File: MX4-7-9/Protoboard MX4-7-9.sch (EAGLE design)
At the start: 444 parts, among them J1 DCJ0202

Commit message: Update to rev2
Updated to Pin headers instead of single wire pads
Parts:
- removed PAD1, PAD10, PAD100, PAD101, PAD102, PAD103, PAD104, PAD105, PAD106, PAD107, PAD108, PAD109, PAD11, PAD110, PAD111, PAD112, PAD113, PAD114, PAD115, PAD116, PAD117, PAD118, PAD119, PAD12, PAD120, PAD121, PAD122, PAD123, PAD124, PAD125, PAD126, PAD127, PAD128, PAD129, PAD13, PAD130, PAD131, PAD132, PAD133, PAD134, PAD135, PAD136, PAD137, PAD138, PAD139, PAD14, PAD140, PAD141, PAD142, PAD143, PAD144, PAD145, PAD146, PAD147, PAD148, PAD149, PAD15, PAD150, PAD151, PAD152, PAD153, PAD154, PAD155, PAD156, PAD157, PAD158, PAD159, PAD16, PAD160, PAD161, PAD162, PAD163, PAD164, PAD165, PAD166, PAD167, PAD168, PAD169, PAD17, PAD170, PAD171, PAD172, PAD173, PAD174, PAD175, PAD176, PAD177, PAD178, PAD179, PAD18, PAD180, PAD181, PAD182, PAD183, PAD184, PAD185, PAD186, PAD187, PAD188, PAD189, PAD19, PAD190, PAD191, PAD192, PAD193, PAD194, PAD195, PAD196, PAD197, PAD198, PAD199, PAD2, PAD20, PAD200, PAD201, PAD202, PAD203, PAD204, PAD205, PAD206, PAD207, PAD208, PAD209, PAD21, PAD210, PAD211, PAD212, PAD213, PAD214, PAD215, PAD216, PAD217, PAD218, PAD219, PAD22, PAD220, PAD221, PAD222, PAD223, PAD224, PAD225, PAD226, PAD227, PAD228, PAD229, PAD23, PAD230, PAD231, PAD232, PAD233, PAD234, PAD235, PAD236, PAD237, PAD238, PAD239, PAD24, PAD240, PAD25, PAD26, PAD260, PAD261, PAD262, PAD263, PAD264, PAD265, PAD266, PAD269, PAD27, PAD270, PAD271, PAD272, PAD273, PAD274, PAD275, PAD276, PAD277, PAD278, PAD279, PAD28, PAD280, PAD281, PAD282, PAD283, PAD284, PAD285, PAD286, PAD287, PAD288, PAD289, PAD29, PAD290, PAD291, PAD292, PAD293, PAD294, PAD295, PAD296, PAD297, PAD298, PAD299, PAD3, PAD30, PAD300, PAD301, PAD302, PAD303, PAD304, PAD305, PAD306, PAD307, PAD308, PAD309, PAD31, PAD310, PAD311, PAD312, PAD313, PAD314, PAD315, PAD316, PAD317, PAD318, PAD319, PAD32, PAD320, PAD321, PAD322, PAD323, PAD324, PAD325, PAD326, PAD327, PAD328, PAD329, PAD33, PAD330, PAD331, PAD332, PAD333, PAD334, PAD335, PAD336, PAD337, PAD338, PAD339, PAD34, PAD340, PAD341, PAD342, PAD343, PAD344, PAD345, PAD346, PAD347, PAD348, PAD349, PAD35, PAD350, PAD351, PAD352, PAD353, PAD354, PAD355, PAD356, PAD357, PAD358, PAD359, PAD36, PAD360, PAD361, PAD362, PAD363, PAD364, PAD365, PAD366, PAD367, PAD368, PAD369, PAD37, PAD370, PAD371, PAD372, PAD373, PAD374, PAD375, PAD376, PAD377, PAD378, PAD379, PAD38, PAD380, PAD381, PAD382, PAD383, PAD384, PAD385, PAD386, PAD387, PAD388, PAD389, PAD39, PAD390, PAD391, PAD392, PAD393, PAD394, PAD395, PAD4, PAD40, PAD41, PAD414, PAD415, PAD416, PAD42, PAD420, PAD421, PAD422, PAD423, PAD424, PAD425, PAD426, PAD427, PAD428, PAD429, PAD43, PAD430, PAD431, PAD432, PAD433, PAD434, PAD435, PAD436, PAD437, PAD438, PAD439, PAD44, PAD440, PAD441, PAD442, PAD443, PAD444, PAD445, PAD446, PAD447, PAD448, PAD449, PAD45, PAD450, PAD451, PAD452, PAD453, PAD454, PAD455, PAD456, PAD457, PAD458, PAD459, PAD46, PAD460, PAD461, PAD462, PAD463, PAD464, PAD465, PAD466, PAD467, PAD468, PAD469, PAD47, PAD470, PAD48, PAD49, PAD5, PAD50, PAD51, PAD52, PAD53, PAD54, PAD55, PAD56, PAD57, PAD58, PAD59, PAD6, PAD60, PAD61, PAD62, PAD63, PAD64, PAD65, PAD66, PAD67, PAD68, PAD69, PAD7, PAD70, PAD71, PAD72, PAD73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: (no value), wirepad:1,6/0,8
- removed PAD471, PAD472, PAD473, PAD474, PAD475, PAD476, PAD477, PAD481, PAD482, PAD483, PAD484, PAD485, PAD486, PAD487: WIREPAD3,17/1,3, wirepad:WIREPAD3,17/1,3
- added J2, J3: (no value), SparkFun-Connectors:M29NO_SILK
- added J4, J5: (no value), SparkFun-Connectors:M20NO_SILK_KIT
- added J6, J7: (no value), SparkFun-Connectors:M05NO_SILK
- added JP1: USB-RECEPTABLE, daspilker:USB-RECEPTABLE
- added JP10, JP11, JP12, JP13, JP14, JP15, JP16, JP17, JP18, JP19, JP2, JP20, JP21, JP22, JP23, JP24, JP25, JP26, JP27, JP28, JP29, JP3, JP30, JP31, JP32, JP33, JP4, JP47, JP5, JP6, JP64, JP65, JP66, JP67, JP68, JP69, JP7, JP70, JP71, JP72, JP73, JP74, JP75, JP76, JP77, JP78, JP79, JP8, JP80, JP81, JP82, JP83, JP9: (no value), adafruit:PINHD-1X6CB
- added JP100, JP101, JP102, JP103, JP104, JP105, JP106, JP107, JP108, JP109, JP34, JP35, JP36, JP37, JP38, JP39, JP40, JP41, JP42, JP43, JP44, JP45, JP46, JP48, JP49, JP50, JP51, JP52, JP53, JP54, JP55, JP56, JP57, JP58, JP59, JP60, JP61, JP62, JP63, JP85, JP86, JP87, JP88, JP89, JP90, JP91, JP92, JP93, JP96, JP97, JP98, JP99: (no value), adafruit:PINHD-1X1CB
- added U2: (no value), SparkFun-PowerIC:MIC52053.3V
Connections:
- removed net N$25: PAD104.P, PAD105.P, PAD113.P, PAD114.P, PAD87.P, PAD95.P, PAD96.P
- removed net N$40: PAD377.P, PAD378.P, PAD379.P, PAD380.P, PAD381.P, PAD382.P, PAD383.P
- removed net N$45: PAD185.P, PAD186.P, PAD194.P, PAD195.P, PAD203.P, PAD204.P, PAD212.P
- removed net N$60: PAD375.P, PAD376.P, PAD384.P, PAD390.P, PAD395.P, PAD414.P, PAD415.P
- removed net N$61: PAD416.P, PAD420.P, PAD437.P, PAD438.P, PAD457.P, PAD458.P, PAD463.P
- removed net N$62: PAD464.P, PAD465.P, PAD466.P, PAD467.P, PAD468.P, PAD469.P, PAD470.P
- removed net N$63: PAD471.P, PAD487.P
- removed net N$64: PAD472.P, PAD486.P
- removed net N$65: PAD473.P, PAD485.P
- removed net N$66: PAD474.P, PAD484.P
- removed net N$67: PAD475.P, PAD483.P
- removed net N$68: PAD476.P, PAD482.P
- removed net N$69: PAD477.P, PAD481.P
- new net N$2: JP31.1, JP31.2, JP31.3, JP31.4, JP31.5, JP31.6, JP96.1
- new net N$46: JP106.1, JP70.1, JP70.2, JP70.3, JP70.4, JP70.5, JP70.6
- new net N$47: JP107.1, JP71.1, JP71.2, JP71.3, JP71.4, JP71.5, JP71.6
- new net N$48: JP108.1, JP72.1, JP72.2, JP72.3, JP72.4, JP72.5, JP72.6
- new net N$52: JP76.1, JP76.2, JP76.3, JP76.4, JP76.5, JP76.6, JP87.1
- new net N$53: JP77.1, JP77.2, JP77.3, JP77.4, JP77.5, JP77.6, JP88.1
- new net N$54: JP78.1, JP78.2, JP78.3, JP78.4, JP78.5, JP78.6, JP89.1
- new net N$55: JP79.1, JP79.2, JP79.3, JP79.4, JP79.5, JP79.6, JP90.1
- new net N$56: JP80.1, JP80.2, JP80.3, JP80.4, JP80.5, JP80.6, JP91.1
- new net N$57: JP81.1, JP81.2, JP81.3, JP81.4, JP81.5, JP81.6, JP92.1
- new net N$58: JP82.1, JP82.2, JP82.3, JP82.4, JP82.5, JP82.6, JP93.1
- net GND: now also J2.1, J2.10, J2.11, J2.12, J2.13, J2.14, J2.15, J2.16, J2.17, J2.18, J2.19, J2.2, J2.20, J2.21, J2.22, J2.23, J2.24, J2.25, J2.26, J2.27, J2.28, J2.29, J2.3, J2.4, J2.5, J2.6, J2.7, J2.8, J2.9, J4.1, J4.10, J4.11, J4.12, J4.13, J4.14, J4.15, J4.16, J4.17, J4.18, J4.19, J4.2, J4.20, J4.3, J4.4, J4.5, J4.6, J4.7, J4.8, J4.9, J6.1, J6.2, J6.3, J6.4, J6.5, JP1.GND, U2.GND; no longer PAD17.P, PAD22.P, PAD23.P, PAD24.P, PAD25.P, PAD26.P, PAD27.P, PAD276.P, PAD277.P, PAD28.P, PAD285.P, PAD286.P, PAD29.P, PAD30.P, PAD31.P, PAD32.P, PAD326.P, PAD327.P, PAD328.P, PAD329.P, PAD33.P, PAD330.P, PAD331.P, PAD339.P, PAD36.P, PAD38.P, PAD4.P, PAD421.P, PAD422.P, PAD423.P, PAD424.P, PAD425.P, PAD426.P, PAD427.P, PAD428.P, PAD429.P, PAD430.P, PAD431.P, PAD432.P, PAD433.P, PAD434.P, PAD435.P, PAD436.P, PAD439.P, PAD440.P, PAD441.P
- net N$1: now also JP2.1, JP2.2, JP2.3, JP2.4, JP2.5, JP2.6, JP48.1; no longer PAD391.P, PAD392.P, PAD393.P, PAD394.P, PAD42.P, PAD43.P, PAD44.P
- net N$10: now also JP54.1, JP9.1, JP9.2, JP9.3, JP9.4, JP9.5, JP9.6; no longer PAD106.P, PAD107.P, PAD108.P, PAD109.P, PAD110.P, PAD111.P, PAD112.P
- net N$11: now also JP10.1, JP10.2, JP10.3, JP10.4, JP10.5, JP10.6, JP55.1; no longer PAD115.P, PAD116.P, PAD117.P, PAD118.P, PAD119.P, PAD120.P, PAD121.P
- net N$12: now also JP11.1, JP11.2, JP11.3, JP11.4, JP11.5, JP11.6, JP56.1; no longer PAD124.P, PAD125.P, PAD126.P, PAD127.P, PAD128.P, PAD129.P, PAD130.P
- net N$13: now also JP12.1, JP12.2, JP12.3, JP12.4, JP12.5, JP12.6, JP57.1; no longer PAD133.P, PAD134.P, PAD135.P, PAD136.P, PAD137.P, PAD138.P, PAD139.P
- net N$14: now also JP13.1, JP13.2, JP13.3, JP13.4, JP13.5, JP13.6, JP58.1; no longer PAD142.P, PAD143.P, PAD144.P, PAD145.P, PAD146.P, PAD147.P, PAD148.P
- net N$15: now also JP14.1, JP14.2, JP14.3, JP14.4, JP14.5, JP14.6, JP59.1; no longer PAD151.P, PAD152.P, PAD153.P, PAD154.P, PAD155.P, PAD156.P, PAD157.P
- net N$16: now also JP15.1, JP15.2, JP15.3, JP15.4, JP15.5, JP15.6, JP60.1; no longer PAD160.P, PAD161.P, PAD162.P, PAD163.P, PAD164.P, PAD165.P, PAD166.P
- net N$17: now also JP16.1, JP16.2, JP16.3, JP16.4, JP16.5, JP16.6, JP61.1; no longer PAD169.P, PAD170.P, PAD171.P, PAD172.P, PAD173.P, PAD174.P, PAD175.P
- net N$18: now also JP4.1, JP4.2, JP4.3, JP4.4, JP4.5, JP4.6, JP62.1; no longer PAD178.P, PAD179.P, PAD180.P, PAD181.P, PAD182.P, PAD183.P, PAD184.P
- net N$19: now also JP17.1, JP17.2, JP17.3, JP17.4, JP17.5, JP17.6, JP63.1; no longer PAD187.P, PAD188.P, PAD189.P, PAD190.P, PAD191.P, PAD192.P, PAD193.P
- net N$20: now also JP18.1, JP18.2, JP18.3, JP18.4, JP18.5, JP18.6, JP34.1; no longer PAD196.P, PAD197.P, PAD198.P, PAD199.P, PAD200.P, PAD201.P, PAD202.P
- net N$21: now also JP19.1, JP19.2, JP19.3, JP19.4, JP19.5, JP19.6, JP35.1; no longer PAD205.P, PAD206.P, PAD207.P, PAD208.P, PAD209.P, PAD210.P, PAD211.P
- net N$22: now also JP20.1, JP20.2, JP20.3, JP20.4, JP20.5, JP20.6, JP36.1; no longer PAD214.P, PAD215.P, PAD216.P, PAD217.P, PAD218.P, PAD219.P, PAD220.P
- net N$23: now also JP47.1, JP47.2, JP47.3, JP47.4, JP47.5, JP47.6, JP99.1; no longer PAD66.P, PAD67.P, PAD68.P, PAD69.P, PAD70.P, PAD71.P, PAD72.P
- net N$24: now also JP100.1, JP64.1, JP64.2, JP64.3, JP64.4, JP64.5, JP64.6; no longer PAD73.P, PAD74.P, PAD75.P, PAD76.P, PAD77.P, PAD78.P, PAD86.P
- net N$26: now also JP101.1, JP65.1, JP65.2, JP65.3, JP65.4, JP65.5, JP65.6; no longer PAD122.P, PAD123.P, PAD131.P, PAD132.P, PAD140.P, PAD141.P, PAD149.P
- net N$27: now also JP21.1, JP21.2, JP21.3, JP21.4, JP21.5, JP21.6, JP37.1; no longer PAD260.P, PAD261.P, PAD262.P, PAD263.P, PAD264.P, PAD265.P, PAD266.P
- net N$28: now also JP22.1, JP22.2, JP22.3, JP22.4, JP22.5, JP22.6, JP38.1; no longer PAD269.P, PAD270.P, PAD271.P, PAD272.P, PAD273.P, PAD274.P, PAD275.P
- net N$29: now also JP23.1, JP23.2, JP23.3, JP23.4, JP23.5, JP23.6, JP39.1; no longer PAD278.P, PAD279.P, PAD280.P, PAD281.P, PAD282.P, PAD283.P, PAD284.P
- net N$3: now also JP32.1, JP32.2, JP32.3, JP32.4, JP32.5, JP32.6, JP97.1; no longer PAD1.P, PAD2.P, PAD3.P, PAD34.P, PAD35.P, PAD37.P, PAD40.P
- net N$30: now also JP24.1, JP24.2, JP24.3, JP24.4, JP24.5, JP24.6, JP40.1; no longer PAD287.P, PAD288.P, PAD289.P, PAD290.P, PAD291.P, PAD292.P, PAD293.P
- net N$31: now also JP25.1, JP25.2, JP25.3, JP25.4, JP25.5, JP25.6, JP41.1; no longer PAD296.P, PAD297.P, PAD298.P, PAD299.P, PAD300.P, PAD301.P, PAD302.P
- net N$32: now also JP26.1, JP26.2, JP26.3, JP26.4, JP26.5, JP26.6, JP42.1; no longer PAD305.P, PAD306.P, PAD307.P, PAD308.P, PAD309.P, PAD310.P, PAD311.P
- net N$33: now also JP27.1, JP27.2, JP27.3, JP27.4, JP27.5, JP27.6, JP43.1; no longer PAD314.P, PAD315.P, PAD316.P, PAD317.P, PAD318.P, PAD319.P, PAD320.P
- net N$34: now also JP102.1, JP66.1, JP66.2, JP66.3, JP66.4, JP66.5, JP66.6; no longer PAD150.P, PAD158.P, PAD159.P, PAD167.P, PAD168.P, PAD176.P, PAD177.P
- net N$35: now also JP28.1, JP28.2, JP28.3, JP28.4, JP28.5, JP28.6, JP44.1; no longer PAD332.P, PAD333.P, PAD334.P, PAD335.P, PAD336.P, PAD337.P, PAD338.P
- net N$36: now also JP29.1, JP29.2, JP29.3, JP29.4, JP29.5, JP29.6, JP45.1; no longer PAD341.P, PAD342.P, PAD343.P, PAD344.P, PAD345.P, PAD346.P, PAD347.P
- net N$37: now also JP30.1, JP30.2, JP30.3, JP30.4, JP30.5, JP30.6, JP46.1; no longer PAD350.P, PAD351.P, PAD352.P, PAD353.P, PAD354.P, PAD355.P, PAD356.P
- net N$38: now also JP103.1, JP67.1, JP67.2, JP67.3, JP67.4, JP67.5, JP67.6; no longer PAD359.P, PAD360.P, PAD361.P, PAD362.P, PAD363.P, PAD364.P, PAD365.P
- net N$39: now also JP104.1, JP68.1, JP68.2, JP68.3, JP68.4, JP68.5, JP68.6; no longer PAD368.P, PAD369.P, PAD370.P, PAD371.P, PAD372.P, PAD373.P, PAD374.P
- net N$4: now also JP33.1, JP33.2, JP33.3, JP33.4, JP33.5, JP33.6, JP98.1; no longer PAD45.P, PAD46.P, PAD47.P, PAD48.P, PAD49.P, PAD50.P, PAD51.P
- net N$41: now also JP105.1, JP69.1, JP69.2, JP69.3, JP69.4, JP69.5, JP69.6; no longer PAD385.P, PAD386.P, PAD387.P, PAD388.P, PAD389.P, PAD39.P, PAD41.P
- net N$49: now also JP109.1, JP73.1, JP73.2, JP73.3, JP73.4, JP73.5, JP73.6; no longer PAD213.P, PAD221.P, PAD222.P, PAD223.P, PAD224.P, PAD225.P, PAD226.P
- net N$5: now also JP3.1, JP3.2, JP3.3, JP3.4, JP3.5, JP3.6, JP49.1; no longer PAD52.P, PAD53.P, PAD54.P, PAD55.P, PAD56.P, PAD57.P, PAD58.P
- net N$50: now also JP74.1, JP74.2, JP74.3, JP74.4, JP74.5, JP74.6, JP85.1; no longer PAD227.P, PAD228.P, PAD229.P, PAD230.P, PAD231.P, PAD232.P, PAD233.P
- net N$51: now also JP75.1, JP75.2, JP75.3, JP75.4, JP75.5, JP75.6, JP86.1; no longer PAD234.P, PAD235.P, PAD236.P, PAD237.P, PAD238.P, PAD239.P, PAD240.P
- net N$59: now also JP83.1, JP83.2, JP83.3, JP83.4, JP83.5, JP83.6; no longer PAD340.P, PAD348.P, PAD349.P, PAD357.P, PAD358.P, PAD366.P, PAD367.P
- net N$6: now also JP5.1, JP5.2, JP5.3, JP5.4, JP5.5, JP5.6, JP50.1; no longer PAD59.P, PAD60.P, PAD61.P, PAD62.P, PAD63.P, PAD64.P, PAD65.P
- net N$7: now also JP51.1, JP6.1, JP6.2, JP6.3, JP6.4, JP6.5, JP6.6; no longer PAD79.P, PAD80.P, PAD81.P, PAD82.P, PAD83.P, PAD84.P, PAD85.P
- net N$8: now also JP52.1, JP7.1, JP7.2, JP7.3, JP7.4, JP7.5, JP7.6; no longer PAD88.P, PAD89.P, PAD90.P, PAD91.P, PAD92.P, PAD93.P, PAD94.P
- net N$9: now also JP53.1, JP8.1, JP8.2, JP8.3, JP8.4, JP8.5, JP8.6; no longer PAD100.P, PAD101.P, PAD102.P, PAD103.P, PAD97.P, PAD98.P, PAD99.P
- net VCC: now also JP1.VCC, U2.EN, U2.IN
- net VDD: now also J3.1, J3.10, J3.11, J3.12, J3.13, J3.14, J3.15, J3.16, J3.17, J3.18, J3.19, J3.2, J3.20, J3.21, J3.22, J3.23, J3.24, J3.25, J3.26, J3.27, J3.28, J3.29, J3.3, J3.4, J3.5, J3.6, J3.7, J3.8, J3.9, J5.1, J5.10, J5.11, J5.12, J5.13, J5.14, J5.15, J5.16, J5.17, J5.18, J5.19, J5.2, J5.20, J5.3, J5.4, J5.5, J5.6, J5.7, J5.8, J5.9, J7.1, J7.2, J7.3, J7.4, J7.5, U2.OUT; no longer PAD10.P, PAD11.P, PAD12.P, PAD13.P, PAD14.P, PAD15.P, PAD16.P, PAD18.P, PAD19.P, PAD20.P, PAD21.P, PAD294.P, PAD295.P, PAD303.P, PAD304.P, PAD312.P, PAD313.P, PAD321.P, PAD322.P, PAD323.P, PAD324.P, PAD325.P, PAD442.P, PAD443.P, PAD444.P, PAD445.P, PAD446.P, PAD447.P, PAD448.P, PAD449.P, PAD450.P, PAD451.P, PAD452.P, PAD453.P, PAD454.P, PAD455.P, PAD456.P, PAD459.P, PAD460.P, PAD461.P, PAD462.P, PAD5.P, PAD6.P, PAD7.P, PAD8.P, PAD9.P
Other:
- moved on the sheet: J1

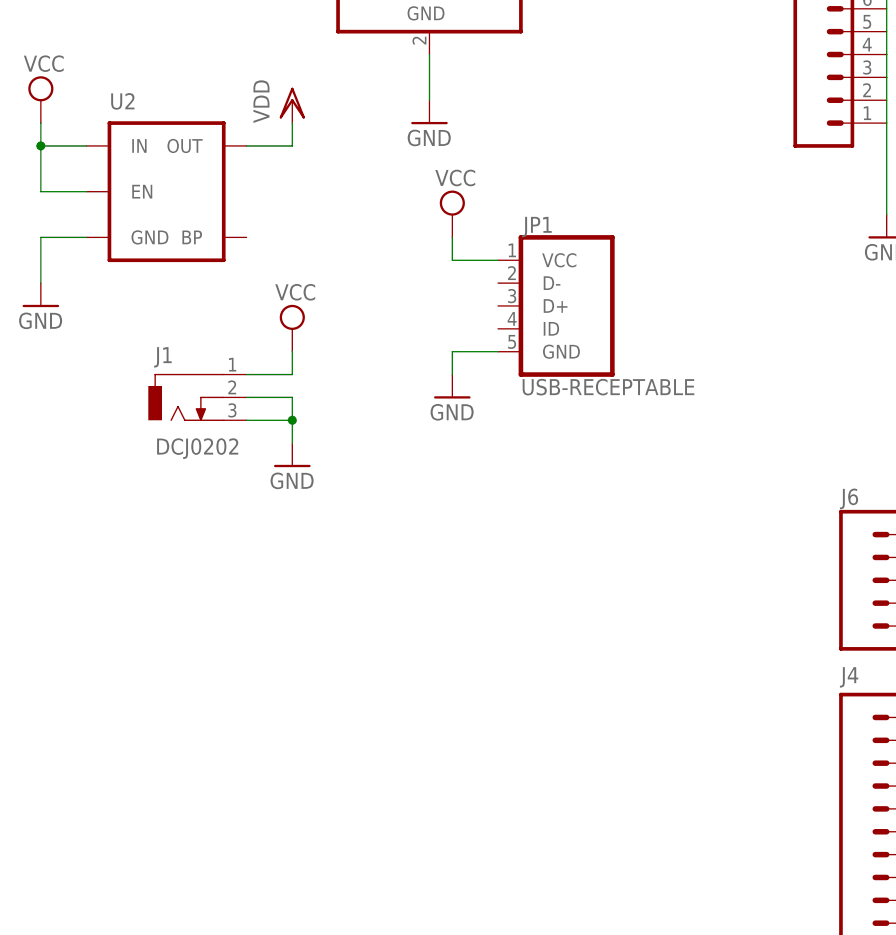
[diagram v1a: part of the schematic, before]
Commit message: Change usb connector
Change to correct usb connecter and moved esp8266 bit more onto the
board.
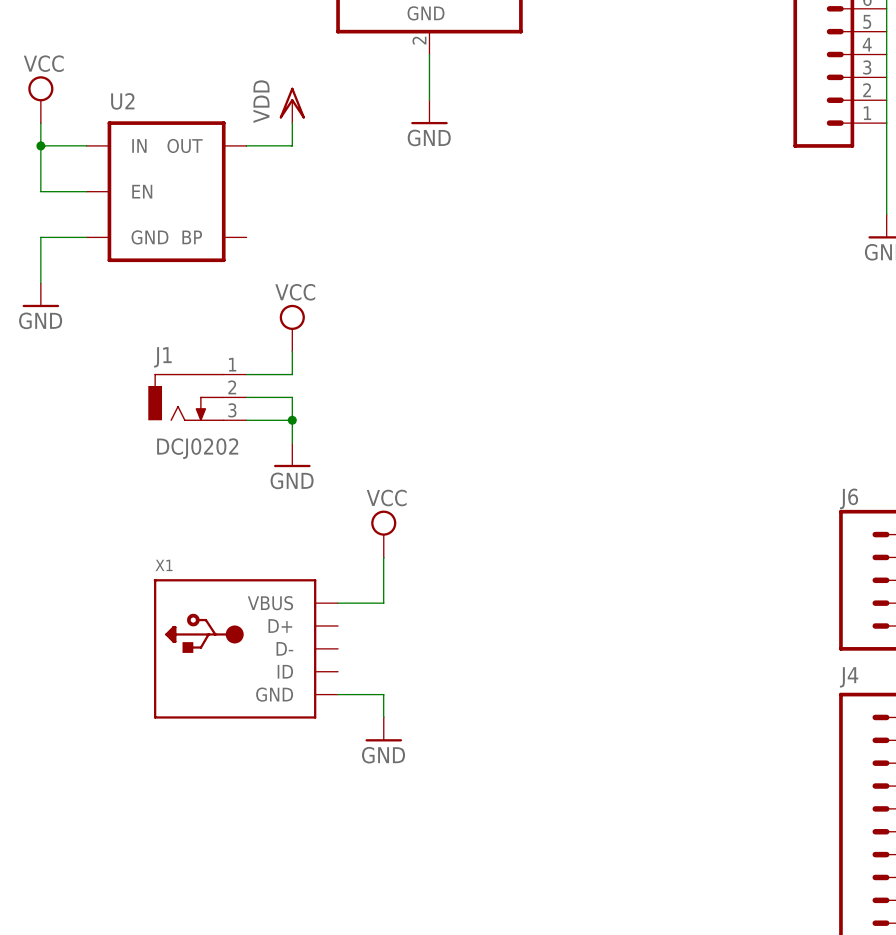
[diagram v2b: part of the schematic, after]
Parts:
- removed JP1: USB-RECEPTABLE, daspilker:USB-RECEPTABLE
- added X1: (no value), microbuilder:USBMICRO_20329
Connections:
- net GND: now also X1.GND; no longer JP1.GND
- net VCC: now also X1.VBUS; no longer JP1.VCC
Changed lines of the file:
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@@
 <part name="SUPPLY4" library="supply2" deviceset="VCC" device=""/>
 <part name="VDD1" library="supply1" deviceset="VDD" device=""/>
-<part name="JP1" library="daspilker" deviceset="USB-RECEPTABLE" device=""/>
-<part name="SUPPLY1" library="supply2" deviceset="VCC" device=""/>
-<part name="GND3" library="supply1" deviceset="GND" device=""/>
 <part name="SUPPLY2" library="supply2" deviceset="VCC" device=""/>
 <part name="GND5" library="supply1" deviceset="GND" device=""/>
@@
 <part name="J6" library="SparkFun-Connectors" deviceset="M05" device="NO_SILK"/>
 <part name="J7" library="SparkFun-Connectors" deviceset="M05" device="NO_SILK"/>
+<part name="X1" library="microbuilder" deviceset="USB" device="MICRO_20329"/>
+<part name="SUPPLY5" library="supply2" deviceset="VCC" device=""/>
+<part name="GND2" library="supply1" deviceset="GND" device=""/>
 </parts>
 <sheets>
@@
 <instance part="SUPPLY4" gate="G$1" x="-45.72" y="66.04"/>
 <instance part="VDD1" gate="G$1" x="-7.62" y="71.12"/>
-<instance part="JP1" gate="G$1" x="-12.7" y="27.94"/>
-<instance part="SUPPLY1" gate="G$1" x="-25.4" y="38.1"/>
-<instance part="GND3" gate="1" x="-25.4" y="17.78"/>
 <instance part="SUPPLY2" gate="G$1" x="-71.12" y="50.8"/>
 <instance part="GND5" gate="1" x="-71.12" y="27.94"/>
@@
 <instance part="J6" gate="G$1" x="20.32" y="-2.54"/>
 <instance part="J7" gate="G$1" x="38.1" y="-2.54"/>
+<instance part="X1" gate="G$1" x="-48.26" y="-10.16"/>
+<instance part="SUPPLY5" gate="G$1" x="-33.02" y="2.54"/>
+<instance part="GND2" gate="1" x="-33.02" y="-20.32"/>
 </instances>
 <busses>
@@
 <pinref part="DC" gate="G$1" pin="GND"/>
 <wire x1="-27.94" y1="50.8" x2="-27.94" y2="55.88" width="0.1524" layer="91"/>
-</segment>
-<segment>
-<pinref part="JP1" gate="G$1" pin="GND"/>
-<pinref part="GND3" gate="1" pin="GND"/>
-<wire x1="-20.32" y1="22.86" x2="-25.4" y2="22.86" width="0.1524" layer="91"/>
-<wire x1="-25.4" y1="22.86" x2="-25.4" y2="20.32" width="0.1524" layer="91"/>
 </segment>
 <segment>
@@
 <wire x1="27.94" y1="0" x2="27.94" y2="2.54" width="0.1524" layer="91"/>
 </segment>
+<segment>
+<pinref part="X1" gate="G$1" pin="GND"/>
+<pinref part="GND2" gate="1" pin="GND"/>
+<wire x1="-38.1" y1="-15.24" x2="-33.02" y2="-15.24" width="0.1524" layer="91"/>
+<wire x1="-33.02" y1="-15.24" x2="-33.02" y2="-17.78" width="0.1524" layer="91"/>
+</segment>
 </net>
 <net name="VCC" class="0">
@@
 <pinref part="DC" gate="G$1" pin="VIN"/>
 <wire x1="-45.72" y1="63.5" x2="-40.64" y2="63.5" width="0.1524" layer="91"/>
-</segment>
-<segment>
-<pinref part="JP1" gate="G$1" pin="VCC"/>
-<pinref part="SUPPLY1" gate="G$1" pin="VCC"/>
-<wire x1="-20.32" y1="33.02" x2="-25.4" y2="33.02" width="0.1524" layer="91"/>
-<wire x1="-25.4" y1="33.02" x2="-25.4" y2="35.56" width="0.1524" layer="91"/>
 </segment>
 <segment>
@@
 <wire x1="-43.18" y1="20.32" x2="-43.18" y2="22.86" width="0.1524" layer="91"/>
 </segment>
+<segment>
+<pinref part="X1" gate="G$1" pin="VBUS"/>
+<pinref part="SUPPLY5" gate="G$1" pin="VCC"/>
+<wire x1="-38.1" y1="-5.08" x2="-33.02" y2="-5.08" width="0.1524" layer="91"/>
+<wire x1="-33.02" y1="-5.08" x2="-33.02" y2="0" width="0.1524" layer="91"/>
+</segment>
 </net>
